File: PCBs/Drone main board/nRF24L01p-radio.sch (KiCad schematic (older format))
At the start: 30 parts, among them J801 SMA-RP, U801 nRF24L01P, U802 RFX2401C, X801 16MHz

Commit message: Redid the radio PCB layout on both drone and remote PCB. Drone PCB had old schematic, remote PCB layout wasn't ideal.
Copied in the VHDL project files from the seperate VHDL project into the main "All in one" project.

Signed-off-by: Eldalote.Electronics <Eldalote.Electronics@gmail.com>
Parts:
- removed C814, C815, C816, C817: 1pF, Capacitor_SMD:C_0402_1005Metric, symbol Device:C_Small
- removed L804, L805: 2.7nH, Inductor_SMD:L_0402_1005Metric, symbol Device:L_Small
- removed R804: 2K, Resistor_SMD:R_0402_1005Metric, symbol Device:R_Small
- removed U801: nRF24L01P, Package_DFN_QFN:QFN-20-1EP_4x4mm_P0.5mm_EP2.5x2.5mm, symbol RF:nRF24L01P
- removed U802: RFX2401C, QFN50P300X300X60-17N-D, symbol SamacSys_Parts:RFX2401C
- added FL801: 2450LP14A100T, SamacSys_Parts:2450LP14A100T, symbol SamacSys_Parts:2450LP14A100T
- added U801: nRF24L01P, Eldalote-footprints:nRF24L01P-QFN-20-1EP_4x4mm_P0.5mm_EP, symbol Eldalote-General:nRF24L01P
- added U802: RFX2401C, Package_DFN_QFN:QFN-16-1EP_3x3mm_P0.5mm_EP1.75x1.75mm, symbol Eldalote-General:RFX2401C
- C801: footprint Capacitor_SMD:C_0402_1005Metric -> Capacitor_SMD:C_0603_1608Metric; LCSC C1585 -> C21117
- C807: footprint Capacitor_SMD:C_0402_1005Metric -> Capacitor_SMD:C_0603_1608Metric_Pad1.05x0.95mm_HandSolder; DigiKey (none) -> 311-1737-1-ND; LCSC C1552 -> (none); Mouser (none) -> 603-CC603BRNPO9BN1R5
- C809: footprint Capacitor_SMD:C_0402_1005Metric -> Capacitor_SMD:C_0603_1608Metric_Pad1.05x0.95mm_HandSolder; DigiKey (none) -> 1276-1095-1-ND; LCSC C1550 -> (none); Mouser (none) -> 187-CL10C010BB8NNNC
- C813: footprint Capacitor_SMD:C_0603_1608Metric -> Capacitor_SMD:C_0603_1608Metric_Pad1.05x0.95mm_HandSolder; LCSC C170140 -> (none)
- J801: value SMA-RP -> SMA
- R802, R803: symbol Device:R_Small -> Device:R
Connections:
- net labels added: RXEN, TXEN
- wire segments 125 -> 109
- no-connect marks 1 -> 0
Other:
- note removed: "A20 B7\nA19 B7\nB22 B6\nC21 B6\nC22 B6\nB20 B7"
- moved on the sheet: C809, C810, C811, C812, C813, J801, R802, R803

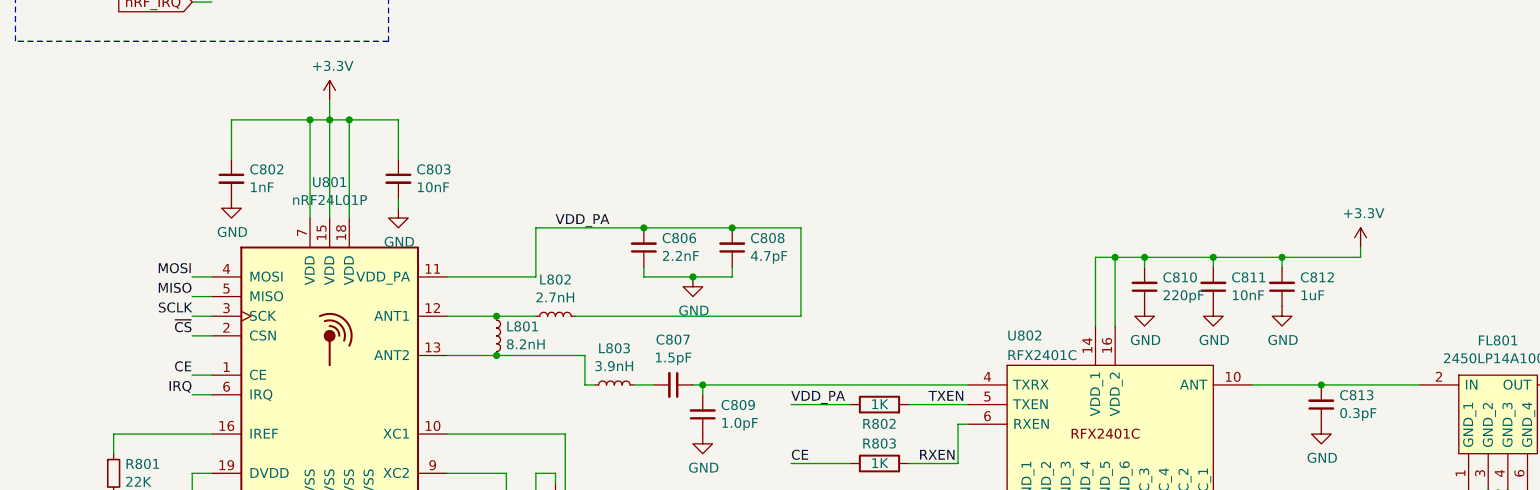
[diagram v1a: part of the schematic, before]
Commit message: Added PDFs of schematics. Corrected a few value labels in drone schematic.
Signed-off-by: Eldalote.Electronics <Eldalote.Electronics@gmail.com>
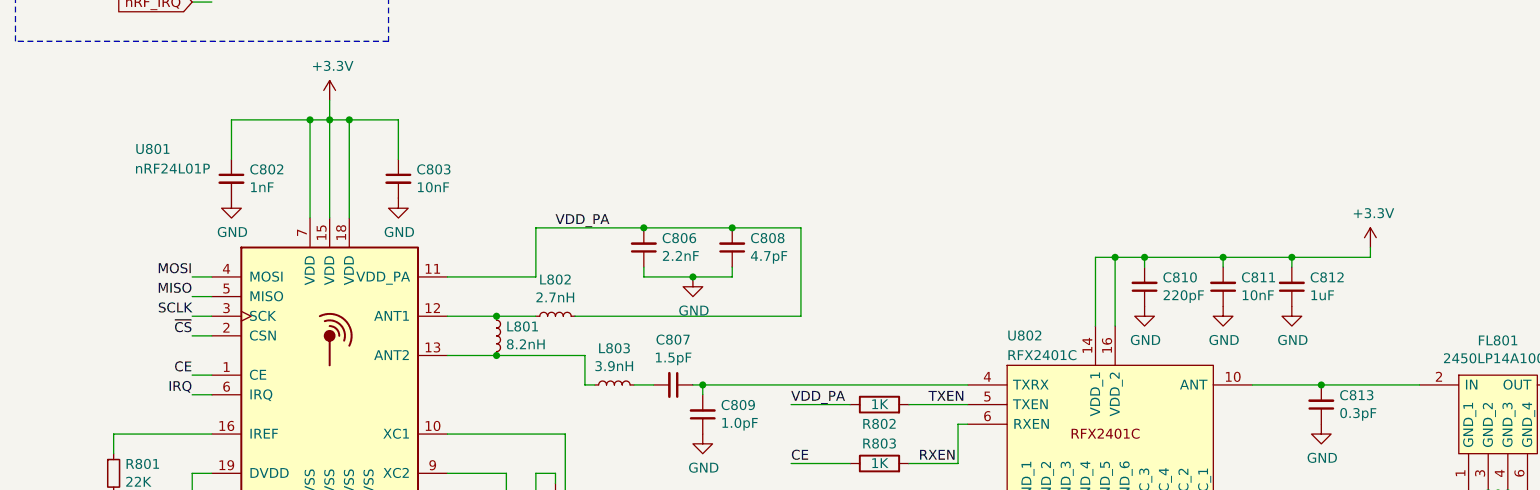
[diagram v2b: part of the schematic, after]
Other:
- moved on the sheet: C811, C812

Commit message: Finished (?) the schematic check and update. Next: PCB update
Signed-off-by: Eldalote.Electronics <Eldalote.Electronics@gmail.com>
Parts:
- added TP801, TP802, TP803, TP804, TP805, TP806: TestPoint, TestPoint:TestPoint_Loop_D2.50mm_Drill1.0mm, symbol Connector:TestPoint
- C801: LCSC C21117 -> (none); MfNr (none) -> CL10B333KB8NNN
- C802: LCSC C1523 -> (none); MfNr (none) -> 04025C102KAT2A
- C803: LCSC C15195 -> (none); MfNr (none) -> 10CL040YF484C6G
- C804, C805: value 15pF -> 8.2pF; LCSC C1548 -> (none); MfNr (none) -> CC0402CRNPO9BN8R2
- C806: LCSC C1531 -> (none); MfNr (none) -> CL05B222JB5NNN
- C807: footprint Capacitor_SMD:C_0603_1608Metric_Pad1.05x0.95mm_HandSolder -> Capacitor_SMD:C_0402_1005Metric; DigiKey 311-1737-1-ND -> (none); MfNr (none) -> CL05C1R5BB5NNN; Mouser 603-CC603BRNPO9BN1R5 -> (none)
- C808: LCSC C1569 -> (none); MfNr (none) -> CC0402CRNPO9BN4R7
- C809: DigiKey 1276-1095-1-ND -> (none); MfNr (none) -> CL10C010BB8NNN; Mouser 187-CL10C010BB8NNNC -> (none)
- C810: LCSC C1530 -> (none); MfNr (none) -> CL05C221JB5NNN
- C811: LCSC C15195 -> (none); MfNr (none) -> CL05B103KB5NNN
- C812: footprint Capacitor_SMD:C_0402_1005Metric -> Capacitor_SMD:C_0603_1608Metric; LCSC C52923 -> (none); MfNr (none) -> CL10A105KB8NNNC
- C813: footprint Capacitor_SMD:C_0603_1608Metric_Pad1.05x0.95mm_HandSolder -> Capacitor_SMD:C_0402_1005Metric; DigiKey 712-1300-1-ND -> (none); MfNr (none) -> 251R07S0R3AV4T; Mouser 609-251R14S0R3AV4T -> (none)
- FL801: DigiKey 712-1129-1-ND -> (none); MfNr (none) -> 2450LP14A100T; Mouser 609-2450LP14A100T -> (none)
- J801: DigiKey CON-SMA-EDGE-S-ND -> (none); MfNr (none) -> CON-SMA-EDGE-S; Mouser 223-CON-SMA-EDGE-S -> (none)
- L801: LCSC C16208 -> (none); MfNr (none) -> HK10058N2J-T
- L802: LCSC C27123 -> (none); MfNr (none) -> MLG1005S2N7BT000
- L803: LCSC C14033 -> (none); MfNr (none) -> MLG1005S3N9BT000
- R801: symbol Device:R_Small -> Device:R; LCSC C25768 -> (none); MfNr (none) -> CR0402-FX-2202GLF
- R802, R803: LCSC C11702 -> (none); MfNr (none) -> RC0402FR-071KL
- U801: DigiKey 1490-1033-1-ND -> (none); LCSC C8791 -> (none); MfNr (none) -> NRF24L01P; Mouser 949-NRF24L01P-T -> (none)
- U802: DigiKey 863-1828-1-ND -> (none); LCSC C19213 -> (none); MfNr (none) -> RFX2401C; Mouser 477-RFX2401C -> (none)
- X801: footprint Crystal:Crystal_SMD_3225-4Pin_3.2x2.5mm -> Eldalote-footprints:Crystal NDK 3.2x2.5; LCSC C13738 -> (none); MfNr (none) -> NX3225SA-16.000M-STD-CSR-1
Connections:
- net nRF_CE: now also TP805.1
- net nRF_CSn: now also TP804.1
- net nRF_IRQ: now also TP806.1
- net nRF_MISO: now also TP802.1
- net nRF_MOSI: now also TP801.1
- net nRF_SCLK: now also TP803.1
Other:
- moved on the sheet: R801

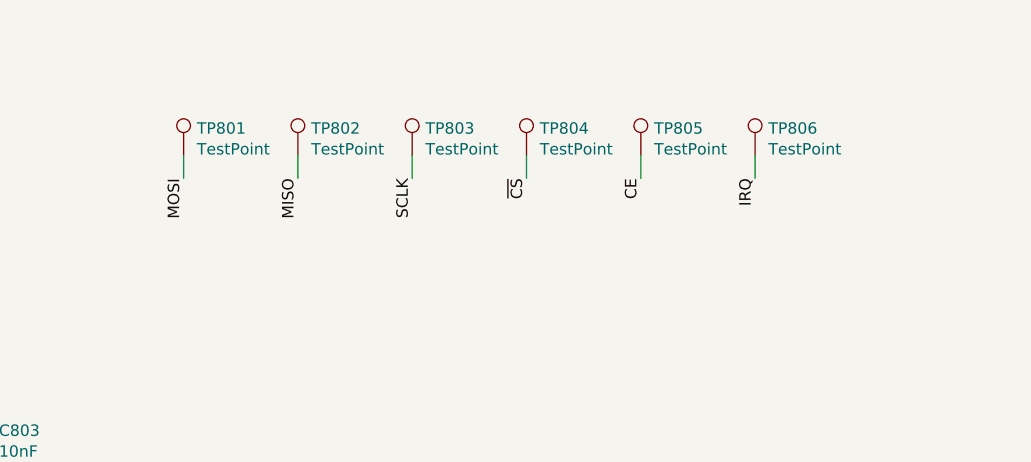
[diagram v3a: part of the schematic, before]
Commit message: Finished redoing PCB.
Signed-off-by: Eldalote.Electronics <Eldalote.Electronics@gmail.com>
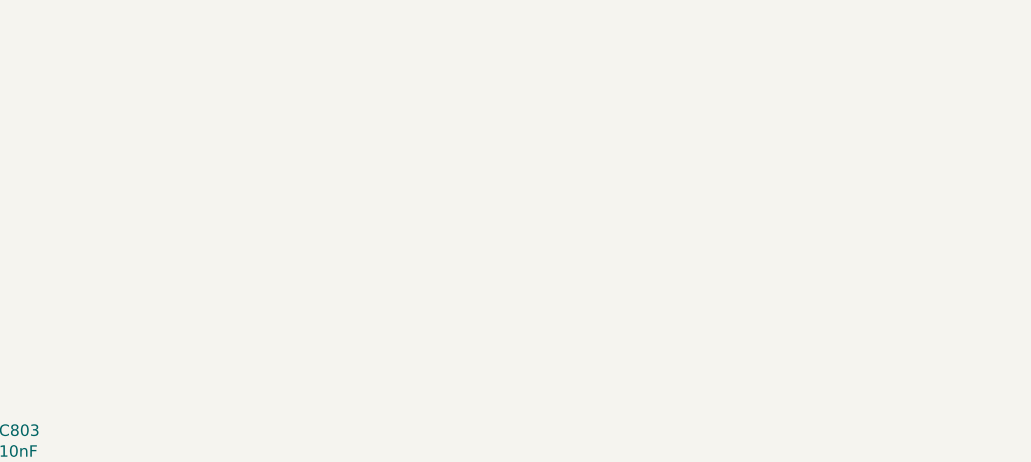
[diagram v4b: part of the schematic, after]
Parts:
- removed TP801, TP802, TP803, TP804, TP805, TP806: TestPoint, TestPoint:TestPoint_Loop_D2.50mm_Drill1.0mm, symbol Connector:TestPoint
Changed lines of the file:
@@
 Text Label 1500 2950 2    50   ~ 0
 MOSI
-Text Label 3950 1300 3    50   ~ 0
-MISO
 Text Label 1500 3150 2    50   ~ 0
 SCLK
@@
 $EndComp
 Connection ~ 6750 2850
-$Comp
-L Connector:TestPoint TP801
-U 1 1 60AF8D62
-P 3450 1200
-F 0 "TP801" H 3508 1318 50  0000 L CNN
-F 1 "TestPoint" H 3508 1227 50  0000 L CNN
-F 2 "TestPoint:TestPoint_Loop_D2.50mm_Drill1.0mm" H 3650 1200 50  0001 C CNN
-F 3 "~" H 3650 1200 50  0001 C CNN
-	1    3450 1200
-	1    0    0    -1
-$EndComp
-$Comp
-L Connector:TestPoint TP804
-U 1 1 60AFE54C
-P 4950 1200
-F 0 "TP804" H 5008 1318 50  0000 L CNN
-F 1 "TestPoint" H 5008 1227 50  0000 L CNN
-F 2 "TestPoint:TestPoint_Loop_D2.50mm_Drill1.0mm" H 5150 1200 50  0001 C CNN
-F 3 "~" H 5150 1200 50  0001 C CNN
-	1    4950 1200
-	1    0    0    -1
-$EndComp
-$Comp
-L Connector:TestPoint TP802
-U 1 1 60AFEA30
-P 3950 1200
-F 0 "TP802" H 4008 1318 50  0000 L CNN
-F 1 "TestPoint" H 4008 1227 50  0000 L CNN
-F 2 "TestPoint:TestPoint_Loop_D2.50mm_Drill1.0mm" H 4150 1200 50  0001 C CNN
-F 3 "~" H 4150 1200 50  0001 C CNN
-	1    3950 1200
-	1    0    0    -1
-$EndComp
-$Comp
-L Connector:TestPoint TP803
-U 1 1 60AFEFB9
-P 4450 1200
-F 0 "TP803" H 4508 1318 50  0000 L CNN
-F 1 "TestPoint" H 4508 1227 50  0000 L CNN
-F 2 "TestPoint:TestPoint_Loop_D2.50mm_Drill1.0mm" H 4650 1200 50  0001 C CNN
-F 3 "~" H 4650 1200 50  0001 C CNN
-	1    4450 1200
-	1    0    0    -1
-$EndComp
-Wire Wire Line
-	3450 1200 3450 1300
-Wire Wire Line
-	3950 1300 3950 1200
-Wire Wire Line
-	4450 1300 4450 1200
-Wire Wire Line
-	4950 1300 4950 1200
-Text Label 3450 1300 3    50   ~ 0
-MOSI
 Text Label 1500 3050 2    50   ~ 0
 MISO
-Text Label 4450 1300 3    50   ~ 0
-SCLK
-Text Label 4950 1300 3    50   ~ 0
-~CS
-$Comp
-L Connector:TestPoint TP805
-U 1 1 60B23A5C
-P 5450 1200
-F 0 "TP805" H 5508 1318 50  0000 L CNN
-F 1 "TestPoint" H 5508 1227 50  0000 L CNN
-F 2 "TestPoint:TestPoint_Loop_D2.50mm_Drill1.0mm" H 5650 1200 50  0001 C CNN
-F 3 "~" H 5650 1200 50  0001 C CNN
-	1    5450 1200
-	1    0    0    -1
-$EndComp
-$Comp
-L Connector:TestPoint TP806
-U 1 1 60B28F74
-P 5950 1200
-F 0 "TP806" H 6008 1318 50  0000 L CNN
-F 1 "TestPoint" H 6008 1227 50  0000 L CNN
-F 2 "TestPoint:TestPoint_Loop_D2.50mm_Drill1.0mm" H 6150 1200 50  0001 C CNN
-F 3 "~" H 6150 1200 50  0001 C CNN
-	1    5950 1200
-	1    0    0    -1
-$EndComp
-Text Label 5450 1300 3    50   ~ 0
-CE
-Wire Wire Line
-	5450 1200 5450 1300
-Wire Wire Line
-	5950 1300 5950 1200
-Text Label 5950 1300 3    50   ~ 0
-IRQ
 $EndSCHEMATC
